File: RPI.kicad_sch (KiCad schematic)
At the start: 48 parts, among them J1 Conn_01x02, J2 Conn_01x04, J3 Conn_01x03, J4 Conn_01x06, J5 GPIO, J6 Conn_01x02, J7 Conn_01x02, J8 Conn_01x02_Male, Q1 DMMT5401-7-F, Q2 DGM2305UX, Q3 SS8050, Q4 IRF9540N, SW1 SW_SPDT, SW2 SW_SPDT, U1 LM2596S-5, U2 LM1085-5.0, U3 AZ431AN-ATRE1

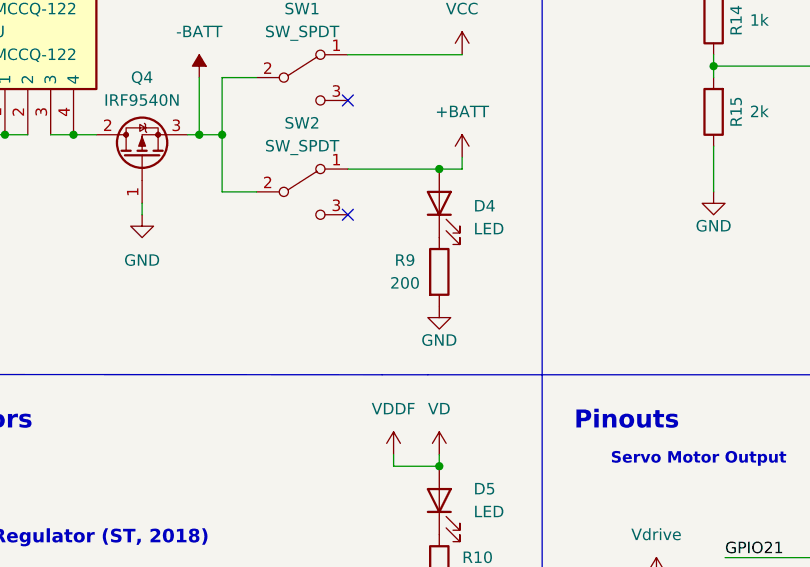
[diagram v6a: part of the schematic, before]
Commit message: Switch input cap to 1210 package for 100uf @16v
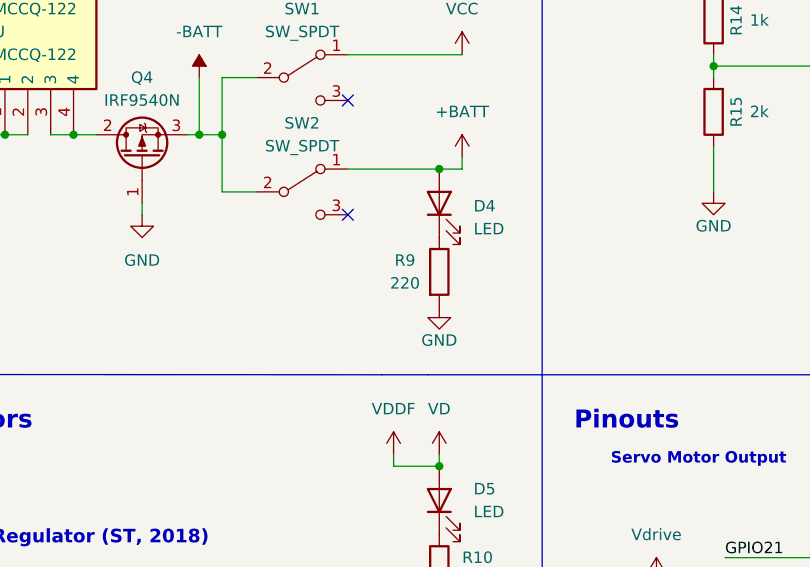
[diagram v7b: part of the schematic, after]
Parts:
- C1: footprint Capacitor_SMD:C_0805_2012Metric_Pad1.18x1.45mm_HandSolder -> Capacitor_SMD:C_1210_3225Metric_Pad1.33x2.70mm_HandSolder
- R9: value 200 -> 220
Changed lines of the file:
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@@
     (in_bom yes) (on_board yes)
     (property "Reference" "R9" (id 0) (at 162.56 55.88 0))
-    (property "Value" "200" (id 1) (at 162.56 58.42 0))
+    (property "Value" "220" (id 1) (at 162.56 58.42 0))
     (property "Footprint" "Resistor_SMD:R_0805_2012Metric_Pad1.20x1.40mm_HandSolder" (id 2) (at 164.592 57.15 90)
       (effects (font (size 1.27 1.27)) hide)
@@
       (effects (font (size 1.27 1.27)) (justify left))
     )
-    (property "Footprint" "Capacitor_SMD:C_0805_2012Metric_Pad1.18x1.45mm_HandSolder" (id 2) (at 93.98 116.84 0)
+    (property "Footprint" "Capacitor_SMD:C_1210_3225Metric_Pad1.33x2.70mm_HandSolder" (id 2) (at 93.98 116.84 0)
       (effects (font (size 1.27 1.27)) hide)
     )
@@
     )
     (path "/c024ec23-528d-4695-84ba-8c9ab497729b"
-      (reference "C1") (unit 1) (value "100u") (footprint "Capacitor_SMD:C_0805_2012Metric_Pad1.18x1.45mm_HandSolder")
+      (reference "C1") (unit 1) (value "100u") (footprint "Capacitor_SMD:C_1210_3225Metric_Pad1.33x2.70mm_HandSolder")
     )
     (path "/544fb3e2-806d-4e28-a55d-c405825c9b95"
@@
     )
     (path "/76cc764a-cfe6-450d-aecc-ffc3000d3d92"
-      (reference "R9") (unit 1) (value "200") (footprint "Resistor_SMD:R_0805_2012Metric_Pad1.20x1.40mm_HandSolder")
+      (reference "R9") (unit 1) (value "220") (footprint "Resistor_SMD:R_0805_2012Metric_Pad1.20x1.40mm_HandSolder")
     )
     (path "/9d5a6be3-2f61-4ec7-8b28-a9e9fa28bf28"

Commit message: Updated drawing info
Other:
- note added: "ROBOTS101 PI-HAT"
- company: (none) -> QUT Robotics Club
- title: (none) -> Robots101 Pi-Hat
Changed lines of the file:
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@@
   (paper "A4")
   (title_block
-    (date "15 nov 2012")
+    (title "Robots101 Pi-Hat")
+    (date "06 / 08 /2023")
+    (rev "2.12")
+    (company "QUT Robotics Club")
+    (comment 1 "By Phoenix Seybold & Stephen Wardle")
   )
   (junction (at 142.24 41.91) (diameter 0) (color 0 0 0 0)
@@
     (effects (font (size 0.7 0.7) italic) (justify left bottom))
   )
+  (text "ROBOTS101 PI-HAT " (at 177.8 175.26 0)
+    (effects (font (size 5 5)) (justify left bottom))
+  )
   (text "Logic shift \nto 3.3v for pi" (at 187.96 149.86 0)
     (effects (font (size 0.7 0.7)) (justify left bottom))
@@
     (effects (font (size 2 2) (thickness 0.4) bold) (justify right bottom))
   )
-  (text "Additional pin functions:\nhttps://pinout.xyz/" (at 179.07 180.34 0)
+  (text "Additional pin functions:\nhttps://pinout.xyz/" (at 259.08 180.34 0)
     (effects (font (size 1.27 1.27)) (justify left bottom))
   )
